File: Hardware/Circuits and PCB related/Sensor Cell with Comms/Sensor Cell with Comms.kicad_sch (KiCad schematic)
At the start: 22 parts, among them J1 Conn_01x02_Shielded, U1 TCAN337, U2 MCP2518FD-xQBB, U3 STM32F103C8Tx, U4 TPS22950x, U5 TPS2421, U6 TPS2421

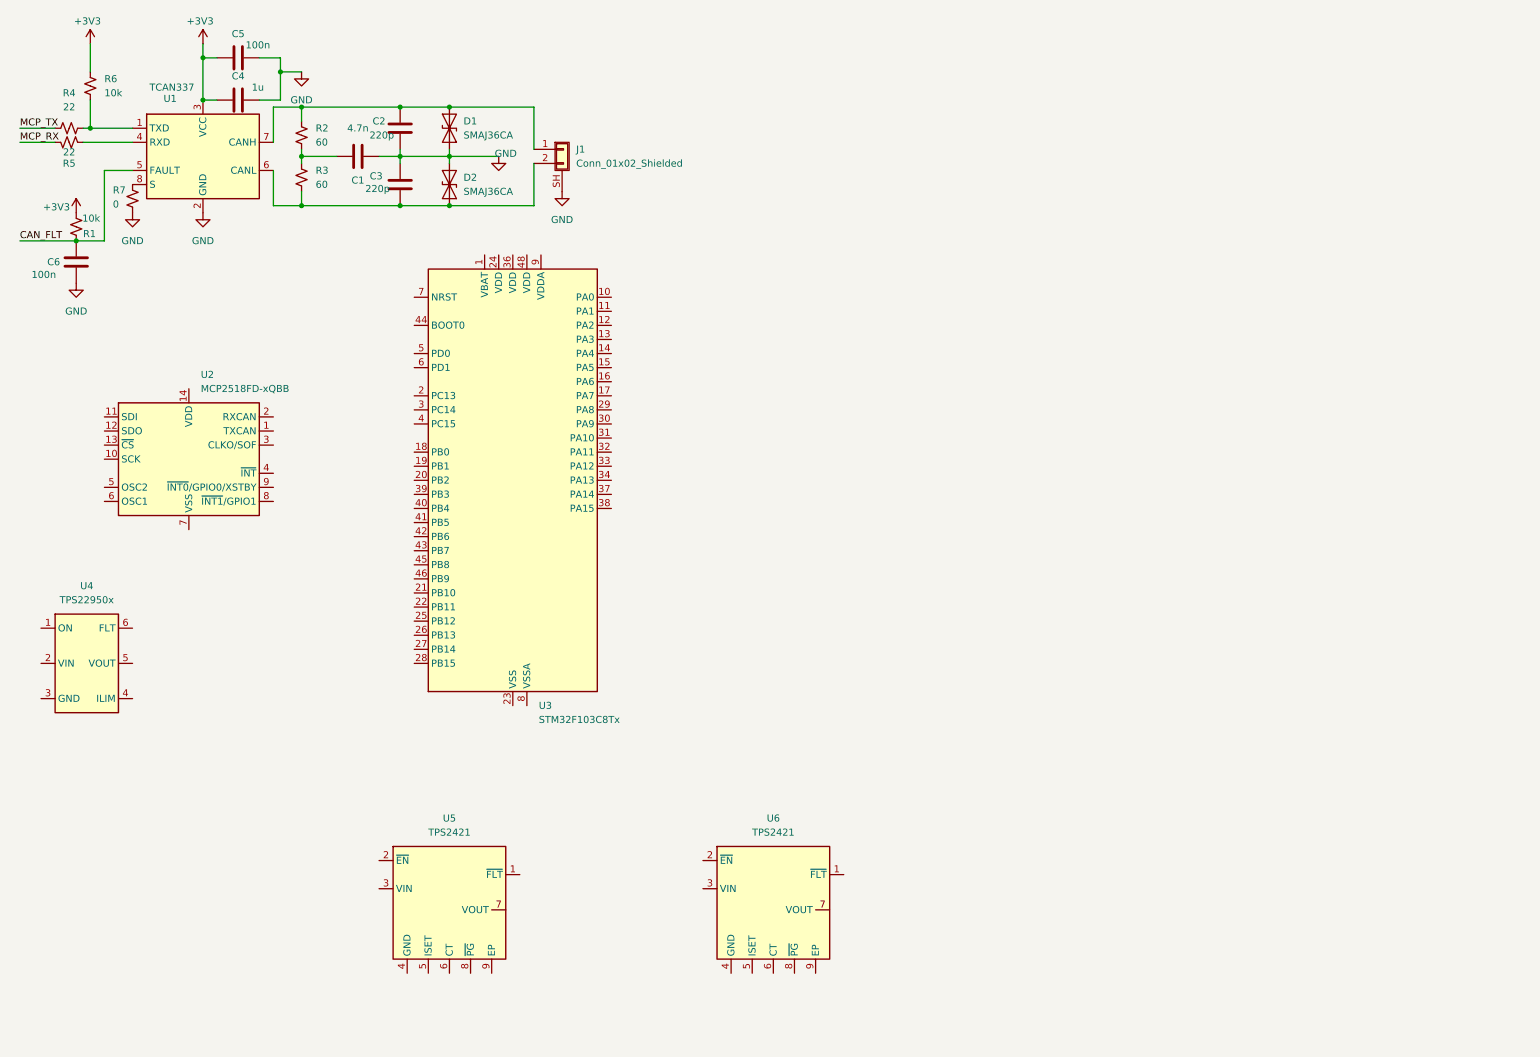
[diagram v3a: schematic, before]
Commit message: hardware re-work mostly done, need to finish EXTq mapping. So far INTs are grouped into 4 banks, PB2,3,4 are reserved, so map those to something else if needed. CAN FLTS is on bank3, Power FLTS is bank 1. Need to finish mapping of additional pins, and then get PCB started. Lastly, I need to finish mapping the OSC pins for MCP and the SOF(start of frame) pin.
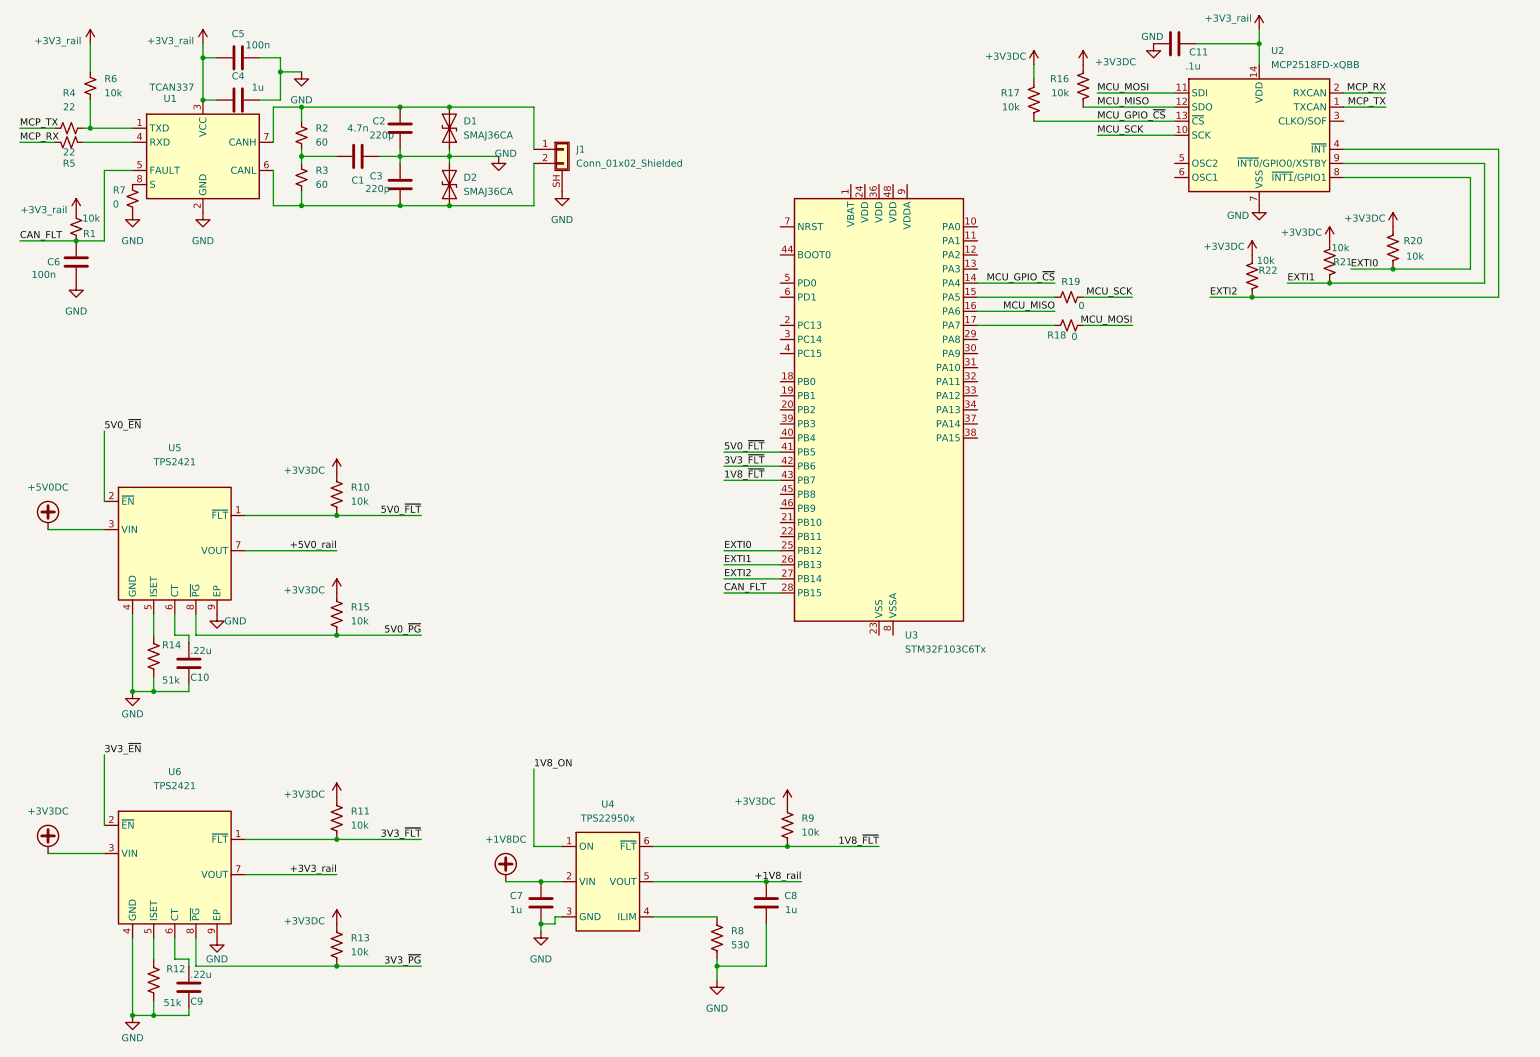
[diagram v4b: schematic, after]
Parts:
- removed U3: STM32F103C8Tx, Package_QFP:LQFP-48_7x7mm_P0.5mm, symbol MCU_ST_STM32F1:STM32F103C8Tx
- added C10, C9: .22u, Capacitor_SMD:C_0603_1608Metric_Pad1.08x0.95mm_HandSolder, symbol Device:C
- added C11: .1u, Capacitor_SMD:C_0603_1608Metric_Pad1.08x0.95mm_HandSolder, symbol Device:C
- added C7, C8: 1u, Capacitor_SMD:C_0603_1608Metric_Pad1.08x0.95mm_HandSolder, symbol Device:C
- added R10, R11, R13, R15, R16, R17, R20, R21, R22, R9: 10k, Resistor_SMD:R_0603_1608Metric_Pad0.98x0.95mm_HandSolder, symbol Device:R_US
- added R12, R14: 51k, Resistor_SMD:R_0603_1608Metric_Pad0.98x0.95mm_HandSolder, symbol Device:R_US
- added R18, R19: 0, Resistor_SMD:R_0603_1608Metric_Pad0.98x0.95mm_HandSolder, symbol Device:R_Small_US
- added R8: 530, Resistor_SMD:R_0603_1608Metric_Pad0.98x0.95mm_HandSolder, symbol Device:R_US
- added U3: STM32F103C6Tx, Package_QFP:LQFP-48_7x7mm_P0.5mm, symbol MCU_ST_STM32F1:STM32F103C6Tx
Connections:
- net +3V3 is gone; now on net +3V3_rail: C4.2, C5.2, R1.1, R6.2, U1.3 (VCC)
- net CAN_FLT: now also U3.28 (PB15)
- net GND: now also U2.15 (VSS), U2.7 (VSS), U4.3 (GND), U5.4 (GND), U5.9 (EP), U6.4 (GND), U6.9 (EP), C10.1, C11.1, C7.1, C8.1, C9.1, R12.1, R14.1, R8.1
- net MCP_RX: now also U2.2 (RXCAN)
- net MCP_TX: now also U2.1 (TXCAN)
- net MCU_SCK: now reaches U2.10 (SCK)
- net MCU_SCK: now also R19.1
- net MCU_MOSI: now reaches U2.11 (SDI)
- net MCU_MOSI: now also R18.1
- net MCU_MISO: now reaches U2.12 (SDO)
- net MCU_MISO: now also R16.1, U3.16 (PA6)
- net MCU_GPIO_~{CS}: now reaches U2.13 (~{CS})
- net MCU_GPIO_~{CS}: now also R17.1, U3.14 (PA4)
- net +3V3_rail: now reaches U2.14 (VDD)
- net +3V3_rail: now also U6.7 (VOUT), C11.2
- net EXTI2: now reaches U2.4 (~{INT})
- net EXTI2: now also R22.1, U3.27 (PB14)
- net EXTI0: now reaches U2.8 (~{INT1}/GPIO1)
- net EXTI0: now also R20.1, U3.25 (PB12)
- net EXTI1: now reaches U2.9 (~{INT0}/GPIO0/XSTBY)
- net EXTI1: now also R21.1, U3.26 (PB13)
- net 3V3_~{FLT}: now reaches U6.1 (~{FLT})
- net 3V3_~{FLT}: now also R11.1, U3.42 (PB6)
- net 3V3_~{EN}: now reaches U6.2 (~{EN})
- net +3V3DC: now reaches U6.3 (VIN)
- net +3V3DC: now also R10.2, R11.2, R13.2, R15.2, R16.2, R17.2, R20.2, R21.2, R22.2, R9.2
- net at U6.5 (ISET): now also R12.2
- net at U6.6 (CT): now also C9.2
- net 3V3_~{PG}: now reaches U6.8 (~{PG})
- net 3V3_~{PG}: now also R13.1
- net 5V0_~{FLT}: now reaches U5.1 (~{FLT})
- net 5V0_~{FLT}: now also R10.1, U3.41 (PB5)
- net 5V0_~{EN}: now reaches U5.2 (~{EN})
- net +5V0DC: now reaches U5.3 (VIN)
- net at U5.5 (ISET): now also R14.2
- net at U5.6 (CT): now also C10.2
- net +5V0_rail: now reaches U5.7 (VOUT)
- net 5V0_~{PG}: now reaches U5.8 (~{PG})
- net 5V0_~{PG}: now also R15.1
- net 1V8_ON: now reaches U4.1 (ON)
- net +1V8DC: now reaches U4.2 (VIN)
- net +1V8DC: now also C7.2
- net at U4.4 (ILIM): now also R8.2
- net +1V8_rail: now reaches U4.5 (VOUT)
- net +1V8_rail: now also C8.2
- net 1V8_~{FLT}: now reaches U4.6 (~{FLT})
- net 1V8_~{FLT}: now also R9.1, U3.43 (PB7)
- new net: R18.2, U3.17 (PA7)
- new net: R19.2, U3.15 (PA5)
- new net: U3.23 (VSS), U3.35 (VSS), U3.47 (VSS)
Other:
- moved on the sheet: U2, U4, U6

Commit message: mostly done with schematic, need to add FRAM chip, ESP<-->STM, and finish the MCP2518 crystal selection and supporting caps for crystal, wants 40 MHz
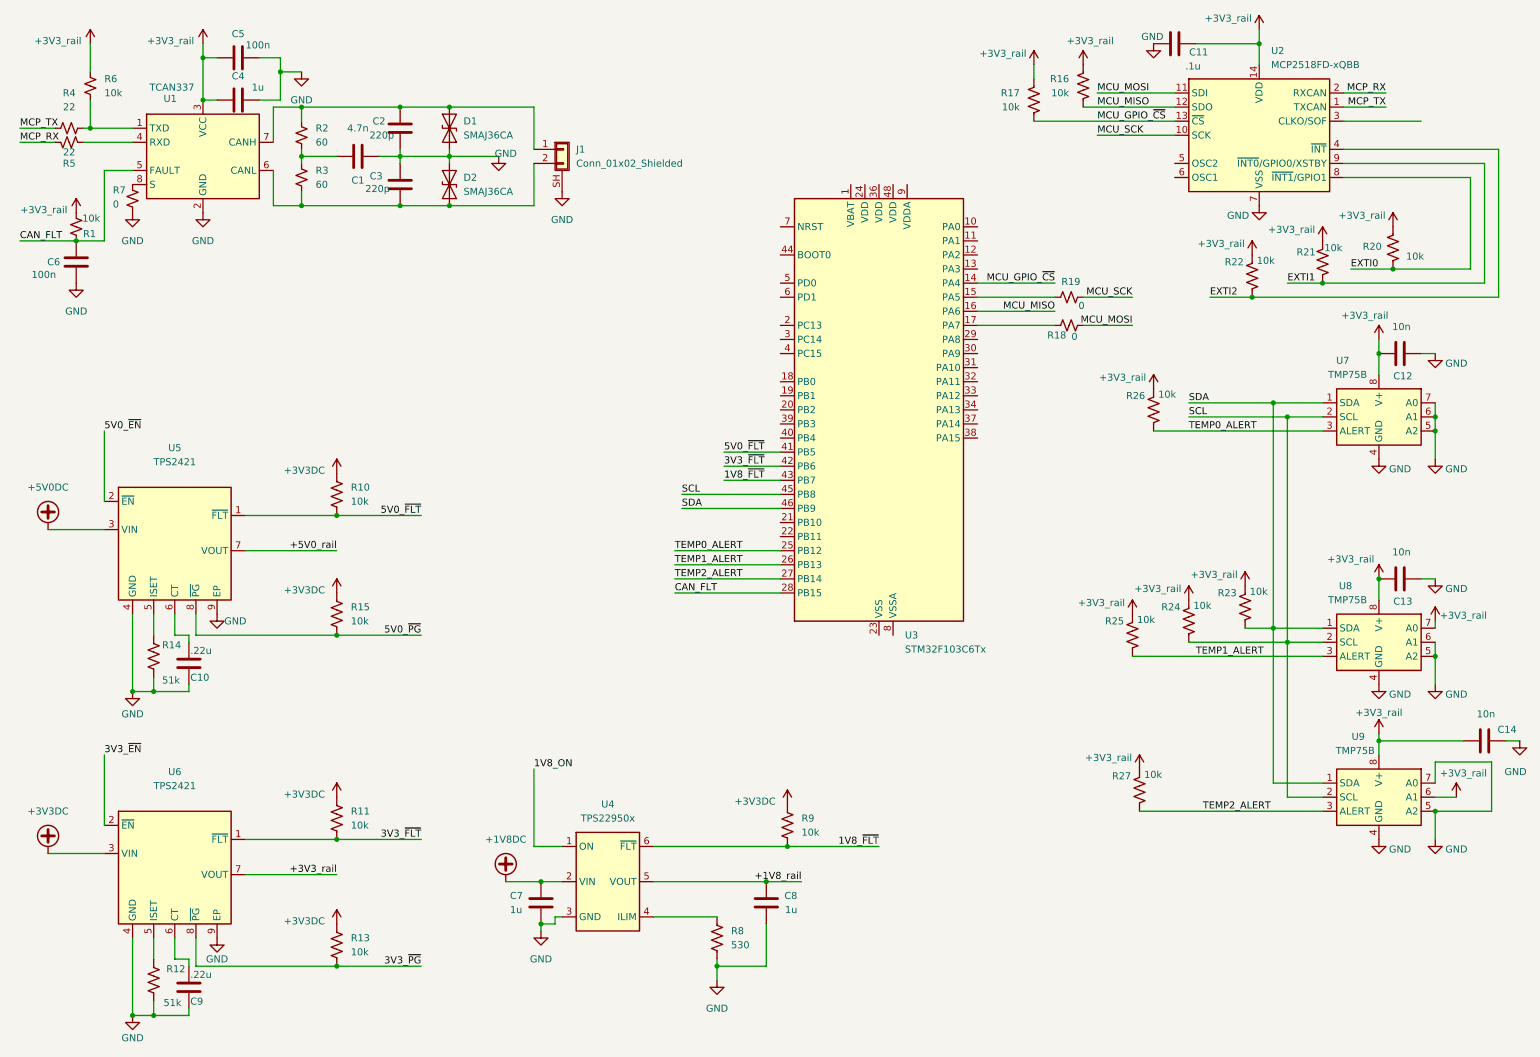
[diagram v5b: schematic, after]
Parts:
- added C12, C13, C14: 10n, Capacitor_SMD:C_0201_0603Metric_Pad0.64x0.40mm_HandSolder, symbol Device:C
- added R23, R24, R25, R26, R27: 10k, Resistor_SMD:R_0603_1608Metric_Pad0.98x0.95mm_HandSolder, symbol Device:R_US
- added U7, U8, U9: TMP75B, Package_SO:SO-8_3.9x4.9mm_P1.27mm, symbol Sensor_Temperature:TMP1075D
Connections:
- net +3V3DC: no longer R16.2, R17.2, R20.2, R21.2, R22.2
- net +3V3_rail: now also R16.2, R17.2, R20.2, R21.2, R22.2, C12.2, C13.2, C14.2, R23.2, R24.2, R25.2, R26.2, R27.2, U7.8 (V+), U8.7 (A0), U8.8 (V+), U9.6 (A1), U9.8 (V+)
- net EXTI0: no longer U3.25 (PB12)
- net EXTI1: no longer U3.26 (PB13)
- net EXTI2: no longer U3.27 (PB14)
- net GND: now also C12.1, C13.1, C14.1, U7.4 (GND), U7.5 (A2), U7.6 (A1), U7.7 (A0), U8.4 (GND), U8.5 (A2), U8.6 (A1), U9.4 (GND), U9.5 (A2), U9.7 (A0)
- net SCL: now reaches U3.45 (PB8)
- net SCL: now also R24.1, U7.2 (SCL), U8.2 (SCL), U9.2 (SCL)
- net SDA: now reaches U3.46 (PB9)
- net SDA: now also R23.1, U7.1 (SDA), U8.1 (SDA), U9.1 (SDA)
- new net TEMP0_ALERT: R26.1, U3.25 (PB12), U7.3 (ALERT)
- new net TEMP1_ALERT: R25.1, U3.26 (PB13), U8.3 (ALERT)
- new net TEMP2_ALERT: R27.1, U3.27 (PB14), U9.3 (ALERT)
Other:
- moved on the sheet: R21

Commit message: added files for the oscillator for the MCP, finished wiring connections in general, need to finish the footprint for the osc and then make PCB using the provided autogenerated nets from KICAD
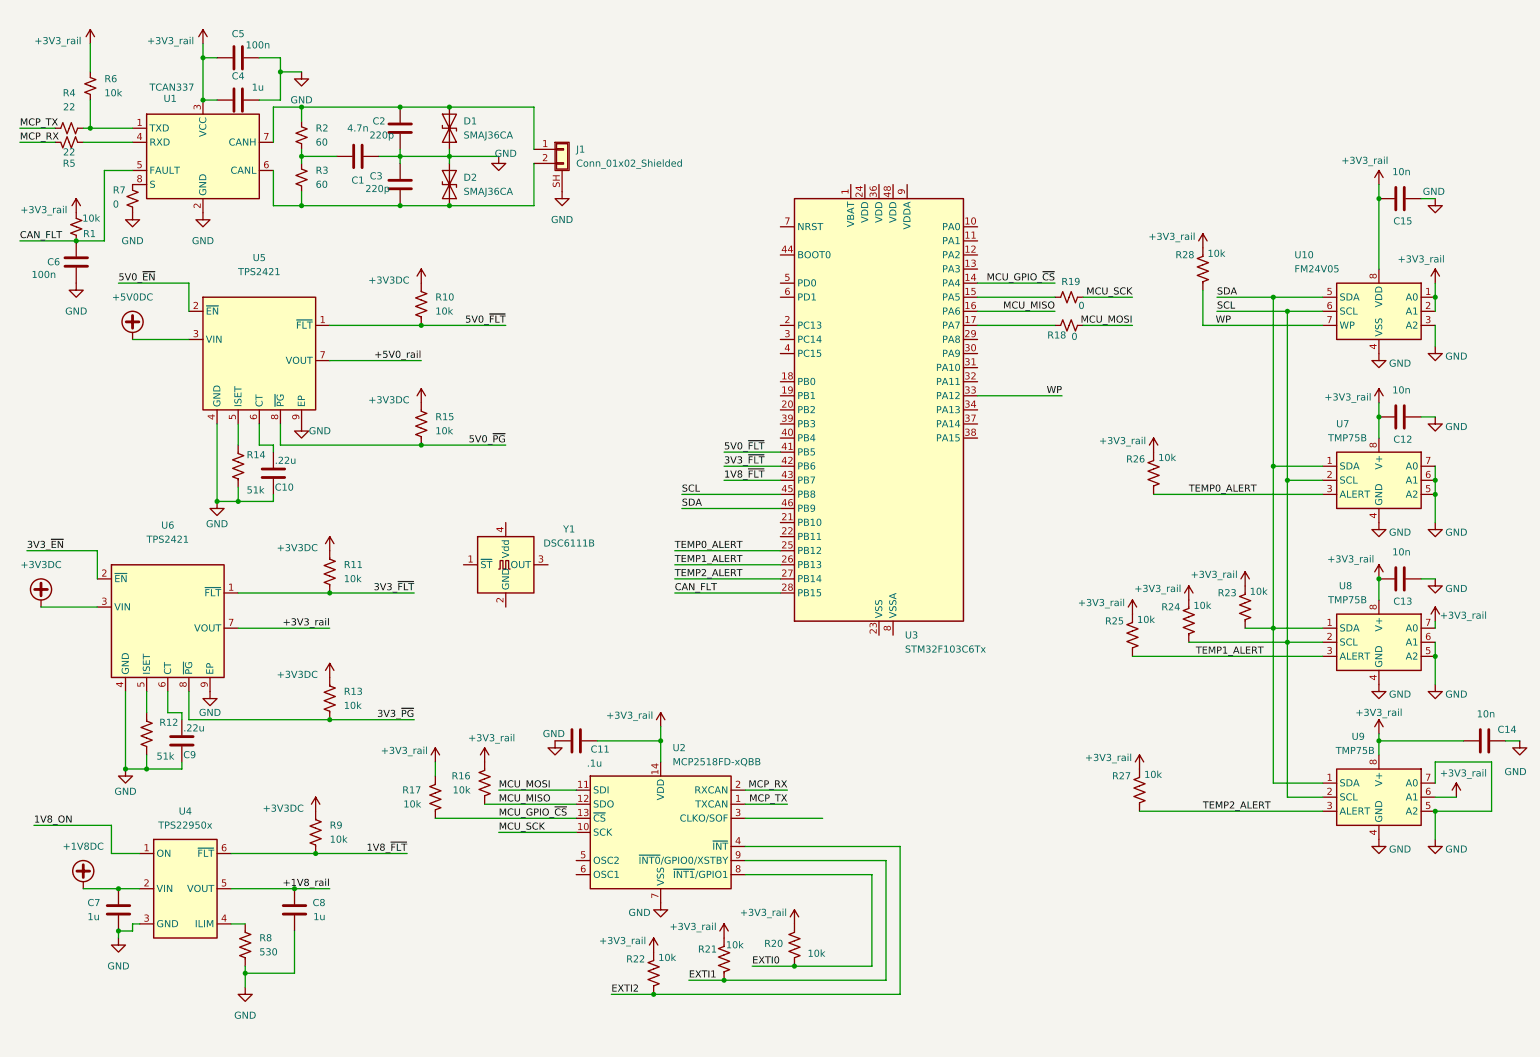
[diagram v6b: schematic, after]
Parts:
- added C15: 10n, Capacitor_SMD:C_0201_0603Metric_Pad0.64x0.40mm_HandSolder, symbol Device:C
- added R28: 10k, Resistor_SMD:R_0603_1608Metric_Pad0.98x0.95mm_HandSolder, symbol Device:R_US
- added U10: FM24V05, Package_SO:SOIC-8_3.9x4.9mm_P1.27mm, symbol Custom Power:FM24V05
- added Y1: DSC6111B, footprintLib:VDFN-4_5x3.2mm_P2.54BSC, symbol Custom Power:DSC61XXB
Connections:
- net +3V3_rail: now also C15.2, R28.2, U10.1 (A0), U10.2 (A1), U10.8 (VDD)
- net GND: now also C15.1, U10.3 (A2), U10.4 (VSS)
- net SCL: now also U10.6 (SCL)
- net SDA: now also U10.5 (SDA)
- net WP: now reaches U3.33 (PA12)
- net WP: now also R28.1, U10.7 (WP)
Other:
- moved on the sheet: C10, C11, C12, C7, C8, C9, R10, R11, R12, R13, R14, R15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
